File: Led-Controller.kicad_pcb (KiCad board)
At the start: 2 copper layers, 51 x 49.2 mm, 43 parts, among them J1 Barrel_Jack, J2 Screw_Terminal, Q1 CSD18540Q5B, Q2 CSD18540Q5B, Q3 CSD18540Q5B, Q4 CSD18540Q5B, Q5 CSD18540Q5B, U1 AMS1117-5.0, U2 AMS1117-3.3, U3 1ED44175N01BXTSA1, U4 1ED44175N01BXTSA1, U5 1ED44175N01BXTSA1, U6 1ED44175N01BXTSA1, U7 1ED44175N01BXTSA1, U8 ESP32-WROOM-32E

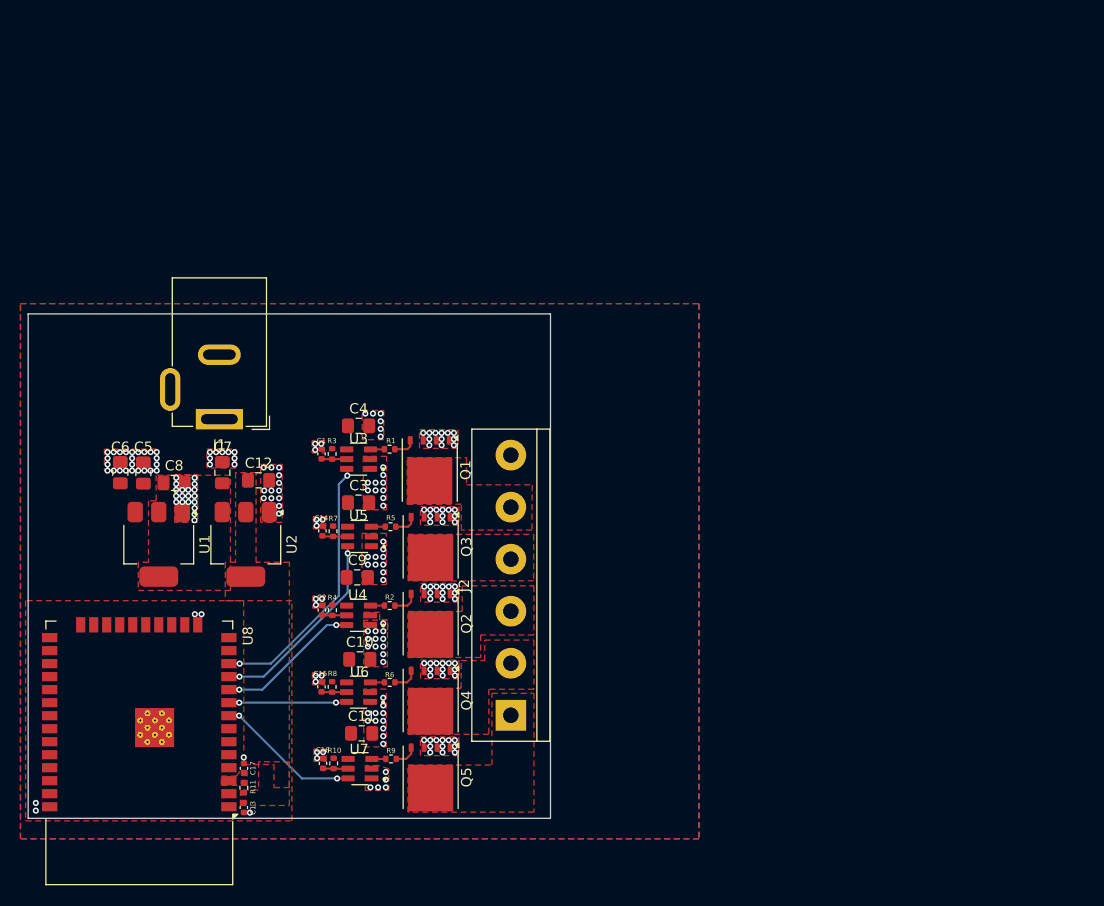
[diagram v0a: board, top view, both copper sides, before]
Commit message: Added: Reverse voltage protection (#19)
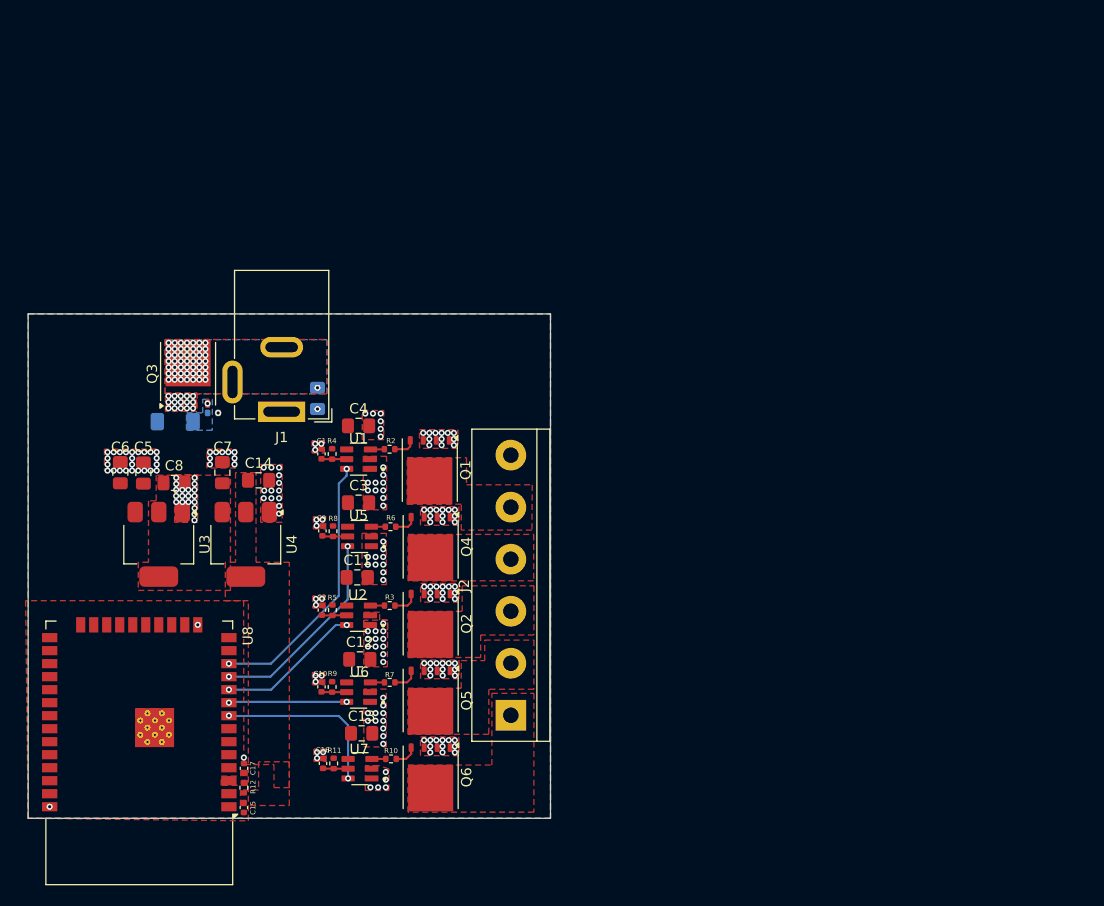
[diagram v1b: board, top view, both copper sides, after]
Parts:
- added C18: 22uf, Capacitor_SMD:C_0805_2012Metric_Pad1.18x1.45mm_HandSolder, B.Cu at (100.5, 96.8)
- added D1: ZMM7v5, Diode_SMD:D_MiniMELF, B.Cu at (86.6, 99.0)
- added Q3: CSD18540Q5B, Package_TO_SOT_SMD:TDSON-8-1, F.Cu at (87.9, 94.3)
- added R1: 100Ω, Resistor_SMD:R_0402_1005Metric, B.Cu at (90.3, 98.2)
- R12: renamed from R11; value 10k -> 10kΩ
- R4: renamed from R3; value 10k -> 10kΩ
- moved J1 6.12 mm to (97.0, 98.0)
- renumbered C15 to C10, C9 to C11, C10 to C12, C11 to C13, C12 to C14, C13 to C15, C14 to C9, Q3 to Q4, Q4 to Q5, Q5 to Q6, R9 to R10, R10 to R11, R1 to R2, R2 to R3, R4 to R5, R5 to R6, R6 to R7, R7 to R8, R8 to R9, U3 to U1, U4 to U2, U1 to U3, U2 to U4
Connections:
- J1 pad 2: GND -> GND1
- J1 pad 3: GND -> GND1
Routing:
- net /IN5: track 14.2 -> 17.2 mm
- net GND: track 0.60 -> 0.03 mm, vias 200 -> 212
- net VCC: track 0.00 -> 0.18 mm, vias 0 -> 2
- net Net-(D1-K): vias 0 -> 1
- net GND1: vias 0 -> 50
- added copper zone on B.Cu, net GND1
- added copper zone on F.Cu, net GND1
- added copper zone on B.Cu, net Net-(D1-K)

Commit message: Added: 6 Pin IDC Connector for Programming (#20)
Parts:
- added J3: Program, Connector_PinHeader_1.27mm:PinHeader_2x03_P1.27mm_Vertical, F.Cu at (78.3, 112.4)
- renumbered C18 to C1, C9 to C10, C10 to C11, C11 to C12, C12 to C13, C13 to C14, C14 to C15, C15 to C16, C16 to C17, C17 to C18, C1 to C2, C2 to C3, C3 to C4, C4 to C5, C5 to C6, C6 to C7, C7 to C8, C8 to C9
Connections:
- net Net-(U8-EN) renamed /EN
- U8 pad 25: unconnected-(U8-IO0-Pad25) -> /BOOT0
- U8 pad 34: unconnected-(U8-RXD0/IO3-Pad34) -> /RX0
- U8 pad 35: unconnected-(U8-TXD0/IO1-Pad35) -> /TX0
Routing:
- net /EN: track 0.24 -> 32.9 mm, vias 0 -> 1
- net +3.3V: track 0.13 -> 32.8 mm, vias 0 -> 1
- net /TX0: track 0.00 -> 25.4 mm, vias 0 -> 1
- net /RX0: track 0.00 -> 19.7 mm, vias 0 -> 1
- net /BOOT0: track 0.00 -> 7.03 mm

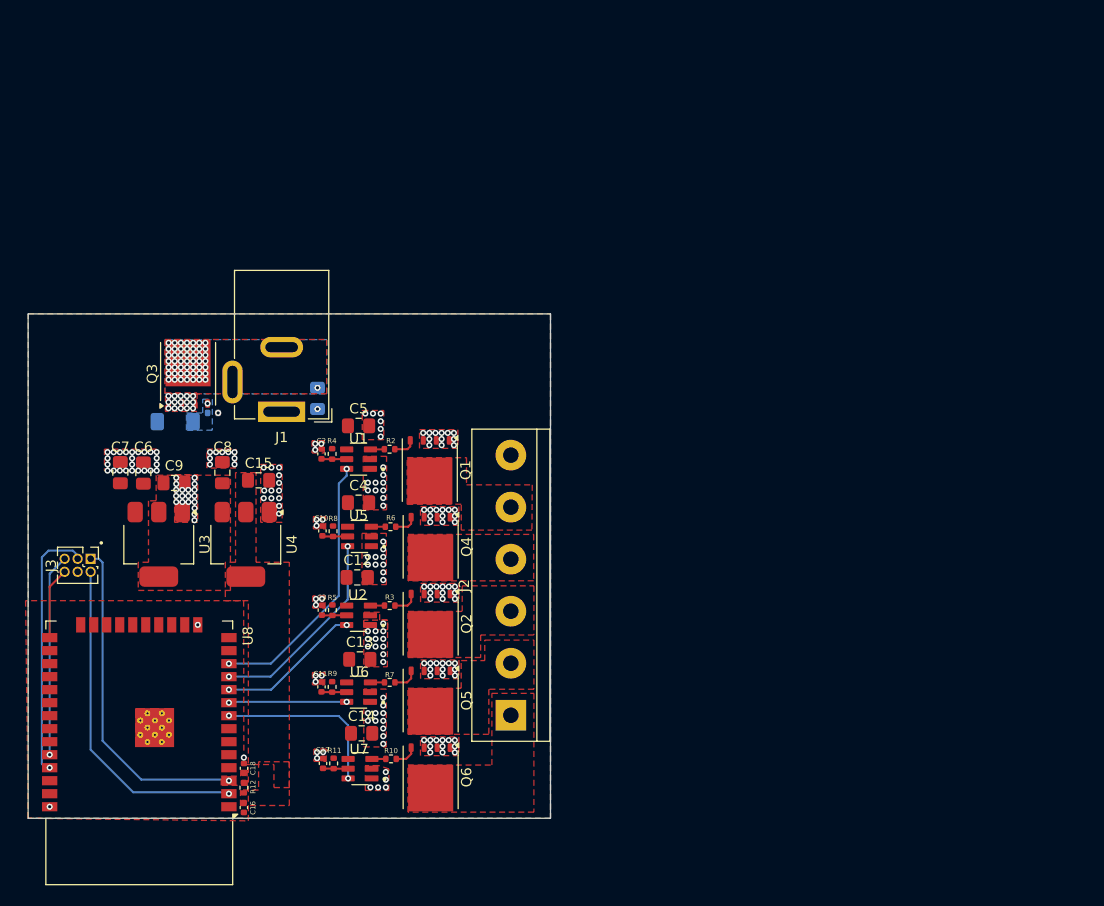
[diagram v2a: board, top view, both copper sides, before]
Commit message: Added: Final Layout for the Switching regulator along with the overall PCB layout
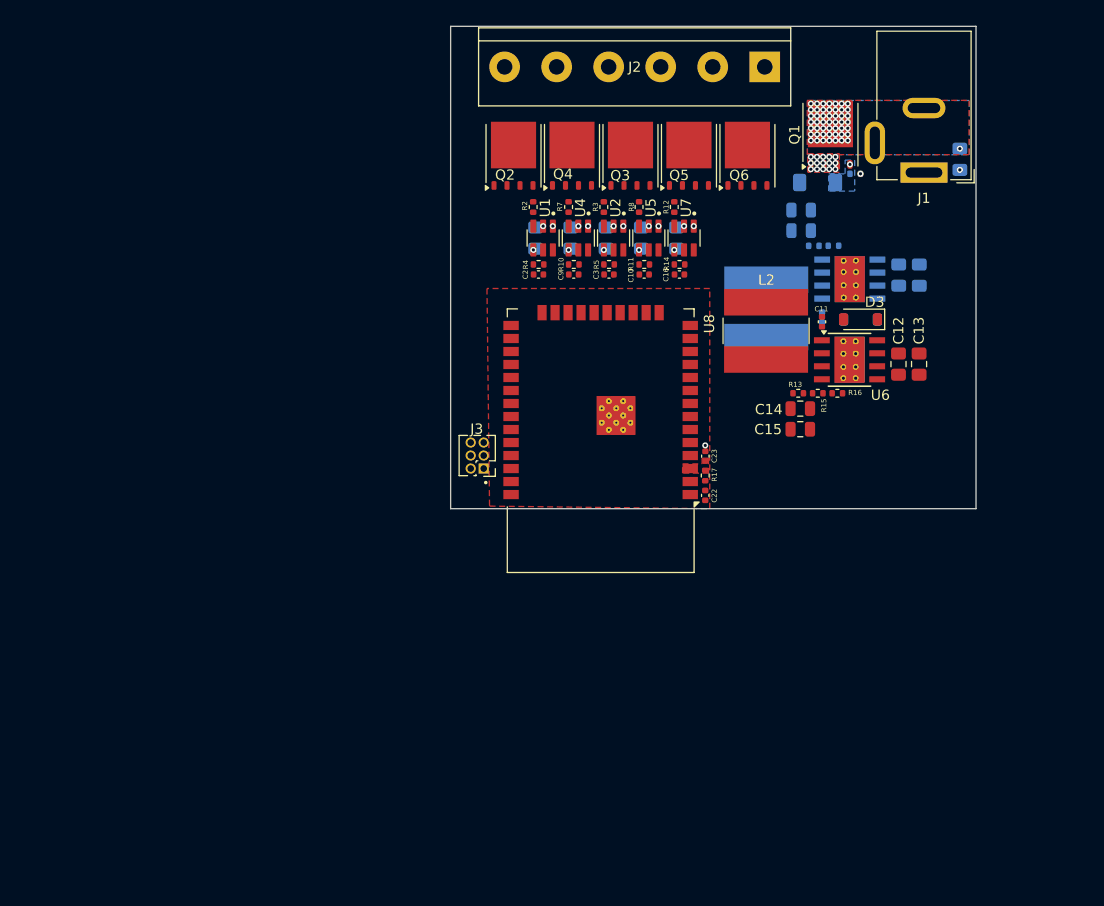
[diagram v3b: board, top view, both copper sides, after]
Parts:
- removed the C6 at (83.5, 104.0)
- removed the C9 at (86.5, 105.0)
- removed the U4 at (93.5, 111.0)
- added C11: 10nf, Capacitor_SMD:C_0402_1005Metric, F.Cu at (149.8, 89.3)
- added C12: 22uf, Capacitor_SMD:C_0805_2012Metric_Pad1.18x1.45mm_HandSolder, F.Cu at (157.2, 93.4)
- added C14: 22uf, Capacitor_SMD:C_0805_2012Metric, F.Cu at (147.6, 97.8)
- added C20: 22uf, Capacitor_SMD:C_0805_2012Metric_Pad1.18x1.45mm_HandSolder, B.Cu at (132.1, 81.1)
- added C21: 22uf, Capacitor_SMD:C_0805_2012Metric_Pad1.18x1.45mm_HandSolder, B.Cu at (135.6, 81.1)
- added C4: 10nf, Capacitor_SMD:C_0402_1005Metric, B.Cu at (149.8, 88.8)
- added C5: 22uf, Capacitor_SMD:C_0805_2012Metric_Pad1.18x1.45mm_HandSolder, B.Cu at (159.3, 84.7)
- added D2: DSK34, Diode_SMD:D_SOD-123, B.Cu at (153.5, 89.0)
- added D3: DSK34, Diode_SMD:D_SOD-123, F.Cu at (153.5, 89.0)
- added L1: 15uH, Inductor_SMD:L_Bourns-SRN8040_8x8.15mm, B.Cu at (144.3, 88.0)
- added L2: 15uH, Inductor_SMD:L_Bourns-SRN8040_8x8.15mm, F.Cu at (144.3, 90.2)
- added R13: 10kΩ, Resistor_SMD:R_0402_1005Metric, F.Cu at (147.4, 96.2)
- added R15: 5.6kΩ, Resistor_SMD:R_0402_1005Metric, F.Cu at (149.3, 96.2)
- added R16: 270Ω, Resistor_SMD:R_0402_1005Metric, F.Cu at (151.3, 96.2)
- added R6: 10kΩ, Resistor_SMD:R_0402_1005Metric, B.Cu at (149.0, 81.9)
- added R9: 1.5kΩ, Resistor_SMD:R_0402_1005Metric, B.Cu at (150.9, 81.8)
- added U6: TPS5430DDA, Package_SO:TI_SO-PowerPAD-8_ThermalVias, F.Cu at (152.4, 93.0)
- C15: footprint Capacitor_SMD:C_0805_2012Metric_Pad1.18x1.45mm_HandSolder -> Capacitor_SMD:C_0805_2012Metric
- C17: renamed from C12; moved to B.Cu
- C18: renamed from C4; moved to B.Cu
- C19: renamed from C5; moved to B.Cu
- C6: renamed from C13; moved to B.Cu
- C7, C8: footprint Capacitor_SMD:C_0805_2012Metric_Pad1.18x1.45mm_HandSolder -> Capacitor_SMD:C_0805_2012Metric; moved to B.Cu
- R10: renamed from R8; value 10k -> 10kΩ
- R11: renamed from R9; value 10k -> 10kΩ
- R14: renamed from R11; value 10k -> 10kΩ
- R5: value 10k -> 10kΩ
- U3: value AMS1117-5.0 -> TPS5430DDA; footprint Package_TO_SOT_SMD:SOT-223-3_TabPin2 -> Package_SO:TI_SO-PowerPAD-8_ThermalVias; moved to B.Cu
- moved U3 72.3 mm to (152.5, 85.1), turned to 0 degrees
- moved C7 70.6 mm to (147.7, 80.4), turned to 180 degrees
- moved Q6 68.1 mm to (142.5, 73.1), turned to 90 degrees
- moved J2 68.0 mm to (144.2, 64.4), turned to 180 degrees
- moved Q1 66.9 mm to (150.6, 71.0)
- moved R1 66.9 mm to (153.0, 74.8)
- moved C1 66.9 mm to (163.2, 73.4)
- moved J1 66.9 mm to (159.7, 74.7)
- moved D1 66.9 mm to (149.3, 75.7)
- moved C13 65.3 mm to (159.2, 93.4), turned to -90 degrees
- moved C6 64.6 mm to (157.3, 84.7), turned to 90 degrees
- moved C8 62.1 mm to (147.7, 78.4), turned to 180 degrees
- moved U7 60.7 mm to (136.3, 81.1), turned to -90 degrees
- moved R12 60.6 mm to (135.3, 78.1), turned to 90 degrees
- moved R14 59.3 mm to (135.8, 83.7), turned to 180 degrees
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- renumbered C11 to C10, C14 to C13, C17 to C16, C16 to C22, C18 to C23, C10 to C9, Q3 to Q1, Q1 to Q2, Q2 to Q3, R10 to R12, R12 to R17, R6 to R7, R7 to R8, U5 to U4, U6 to U5
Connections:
- C15 pad 1: +3.3V -> GND
- C15 pad 2: GND -> +3.3V
- C17 pad 1: VCC -> +9V
- C18 pad 1: VCC -> +9V
- C19 pad 1: VCC -> +9V
- C7 pad 1: VCC -> GND
- C7 pad 2: GND -> +9V
- C8 pad 1: +5V -> GND
- C8 pad 2: GND -> +9V
- J2 pad 1: /OUT5 -> VCC
- J2 pad 2: /OUT4 -> /OUT5
- J2 pad 3: /OUT3 -> /OUT4
- J2 pad 4: /OUT2 -> /OUT3
- J2 pad 5: /OUT1 -> /OUT2
- J2 pad 6: VCC -> /OUT1
- R10 pad 2: VCC -> +9V
- R11 pad 2: VCC -> +9V
- R14 pad 2: VCC -> +9V
- R4 pad 2: VCC -> +9V
- R5 pad 2: VCC -> +9V
- U1 pad 4: VCC -> +9V
- U2 pad 4: VCC -> +9V
- U3 pad 1: GND -> Net-(U3-BOOT)
- U3 pad 2: +5V -> unconnected-(U3-NC-Pad2)
- U3 pad 3: VCC -> unconnected-(U3-NC-Pad3)
- U4 pad 4: VCC -> +9V
- U5 pad 4: VCC -> +9V
- U7 pad 4: VCC -> +9V
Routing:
- net /EN: track 32.9 -> 0.24 mm, vias 1 -> 0
- net +3.3V: track 32.8 -> 0.13 mm, vias 1 -> 0
- net /IN1: track 26.3 -> 0.08 mm, vias 2 -> 0
- net /TX0: track 25.4 -> 0.00 mm, vias 1 -> 0
- net /IN2: track 20.0 -> 0.04 mm, vias 2 -> 0
- net /RX0: track 19.7 -> 0.00 mm, vias 1 -> 0
- net /IN5: track 17.2 -> 0.03 mm, vias 2 -> 0
- net /IN3: track 14.1 -> 0.01 mm, vias 2 -> 0
- net /IN4: track 11.6 -> 0.01 mm, vias 2 -> 0
- net /BOOT0: track 7.03 -> 0.00 mm
- net Net-(Q3-G): track 2.51 -> 0.00 mm
- net Net-(Q5-G): track 2.49 -> 0.00 mm
- net Net-(U5-EN/~{FLT}): track 2.47 -> 0.00 mm
- net Net-(U7-EN/~{FLT}): track 2.46 -> 0.00 mm
- net Net-(U1-EN/~{FLT}): track 2.47 -> 0.04 mm
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- removed copper zone on F.Cu, net +3.3V
- removed copper zone on F.Cu, net +5V
- removed copper zone on F.Cu, net /OUT1
- removed copper zone on F.Cu, net /OUT2
- removed copper zone on F.Cu, net /OUT3
- removed copper zone on F.Cu, net /OUT4
- removed copper zone on F.Cu, net /OUT5
- removed copper zone on B.Cu, net GND
- removed copper zone on F.Cu, net VCC
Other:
- board size 51 x 49.2 mm -> 51.3 x 47.1 mm

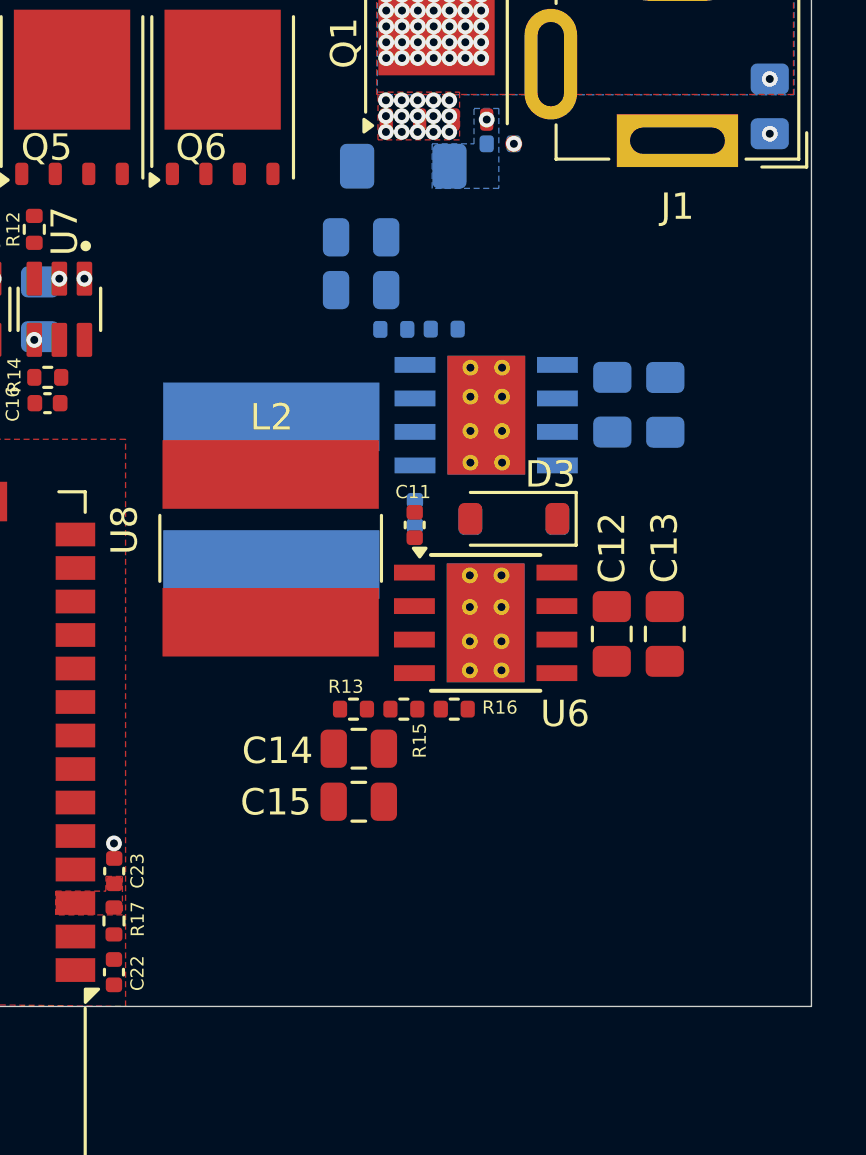
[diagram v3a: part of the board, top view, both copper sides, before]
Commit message: Added: Ferrite bead for conduction EMI filtering
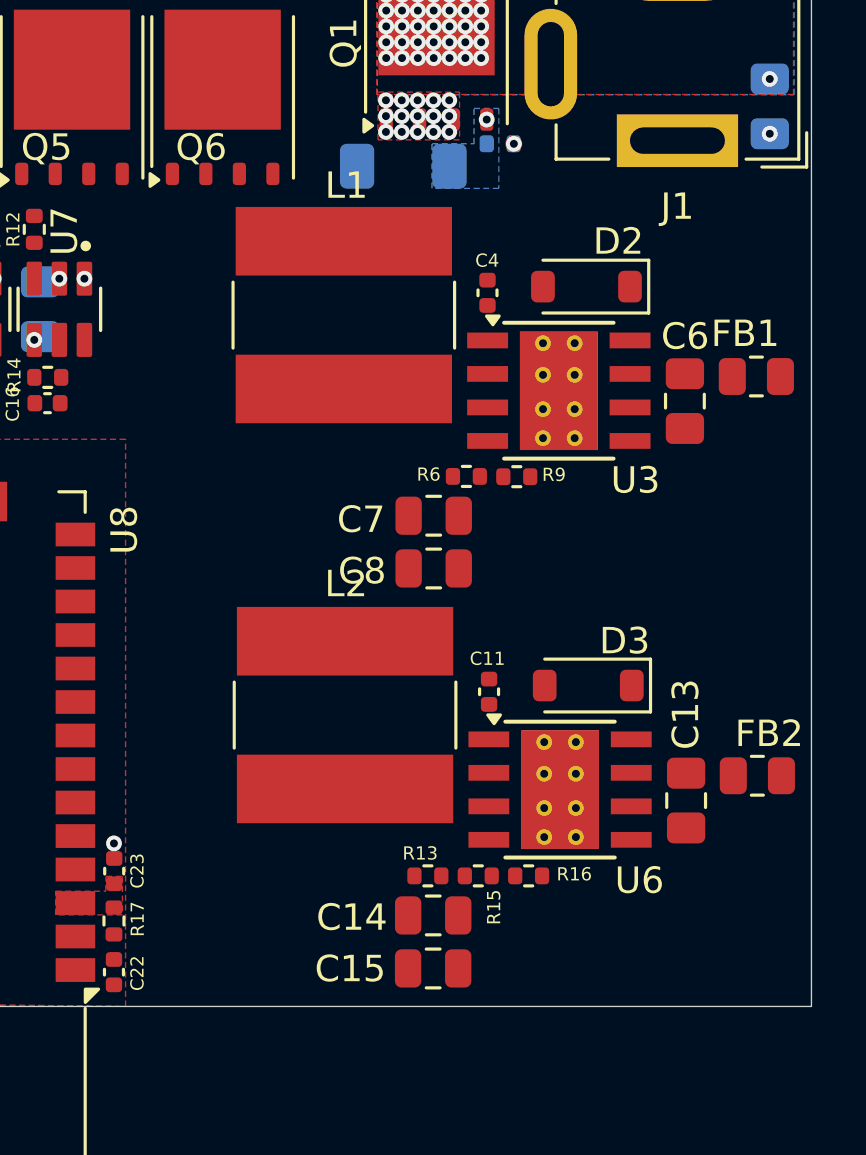
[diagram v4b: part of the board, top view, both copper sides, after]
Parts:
- removed C12, C5: 22uf, Capacitor_SMD:C_0805_2012Metric_Pad1.18x1.45mm_HandSolder
- added FB1: 220Ω, Resistor_SMD:R_0805_2012Metric, F.Cu at (162.7, 83.6)
- added FB2: 220Ω, Resistor_SMD:R_0805_2012Metric, F.Cu at (162.8, 98.8)
- C4, C6, C7, C8, D2, L1, R6, R9, U3: moved to F.Cu
- moved C8 12.9 mm to (150.5, 90.9)
- moved D2 9.24 mm to (156.3, 80.2)
- moved C7 8.98 mm to (150.5, 88.9)
- moved C4 8.79 mm to (152.5, 80.5), turned to 90 degrees
- moved L1 7.20 mm to (147.1, 81.3), turned to -90 degrees
- moved C11 6.92 mm to (152.6, 95.6)
- moved D3 6.92 mm to (156.3, 95.4)
- moved C15 6.92 mm to (150.5, 106.1)
- moved R16 6.92 mm to (154.1, 102.6)
- moved U6 6.92 mm to (155.3, 99.3)
- moved C14 6.92 mm to (150.5, 104.1)
- moved L2 6.92 mm to (147.1, 96.5)
- moved R13 6.92 mm to (150.3, 102.6)
- moved R15 6.92 mm to (152.2, 102.6)
- moved C13 6.37 mm to (160.1, 99.7)
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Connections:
- C13 pad 1: VCC -> Net-(U6-VIN)
- C6 pad 1: VCC -> Net-(U3-VIN)
- U3 pad 7: VCC -> Net-(U3-VIN)
- U6 pad 7: VCC -> Net-(U6-VIN)
